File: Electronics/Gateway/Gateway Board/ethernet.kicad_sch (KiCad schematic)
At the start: 24 parts, among them IC6 LAN8742A-CZ-TR, J4 HR913129A, U1 USBLC6-4SC6-ES

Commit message: PCB Schematics finished
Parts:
- renumbered C18 to C401, C16 to C402, C17 to C403, C13 to C404, C19 to C405, C14 to C406, C15 to C407, FB1 to FB401, IC6 to IC401, J4 to J401, R22 to R401, R26 to R402, R27 to R403, R25 to R404, R32 to R405, R33 to R406, R21 to R407, R17 to R408, R18 to R409, R20 to R410, R19 to R411, R23 to R412, R24 to R413

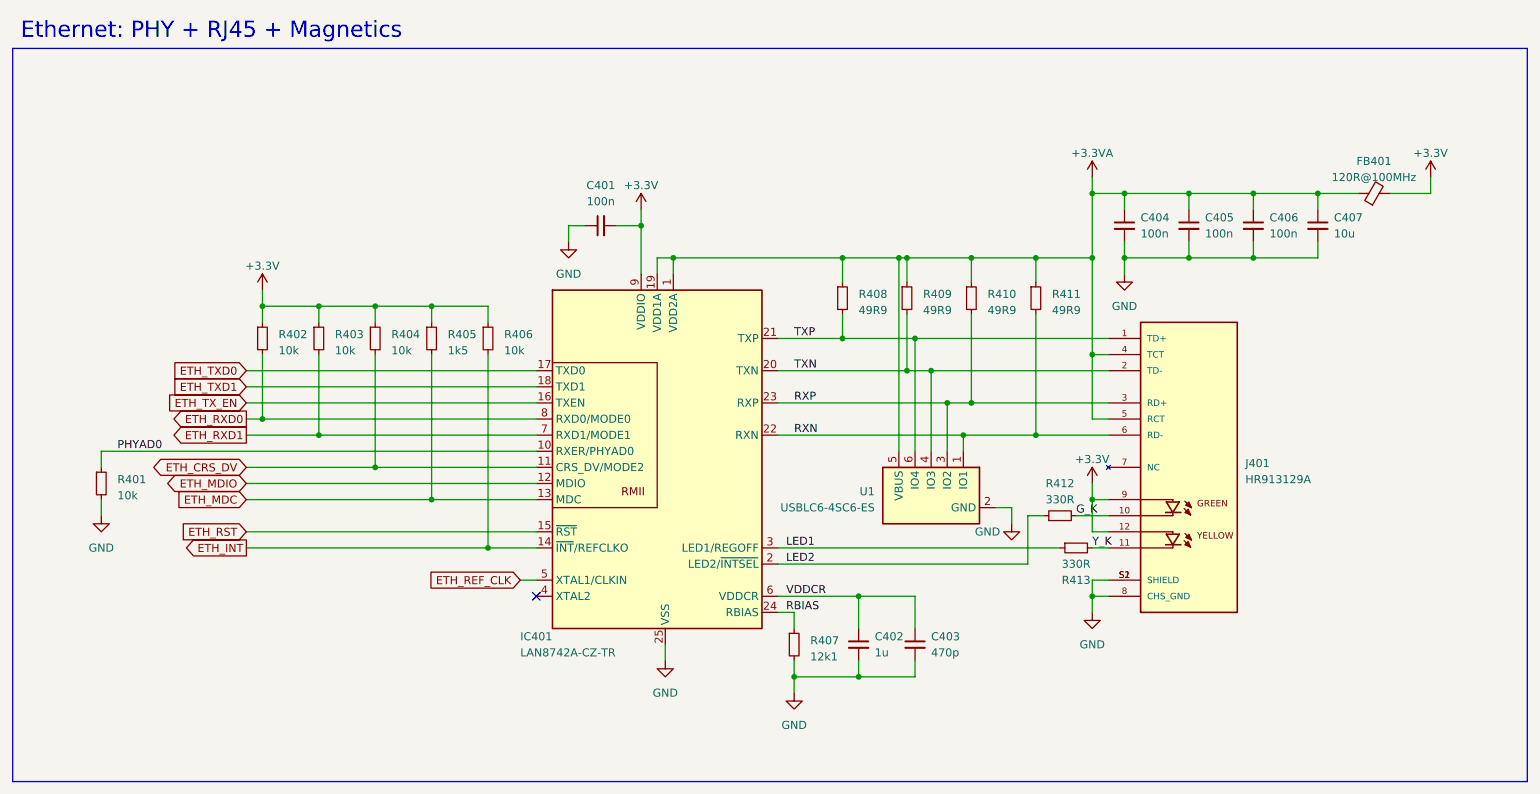
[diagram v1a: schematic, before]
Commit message: Gateway board layout complete and routing begun
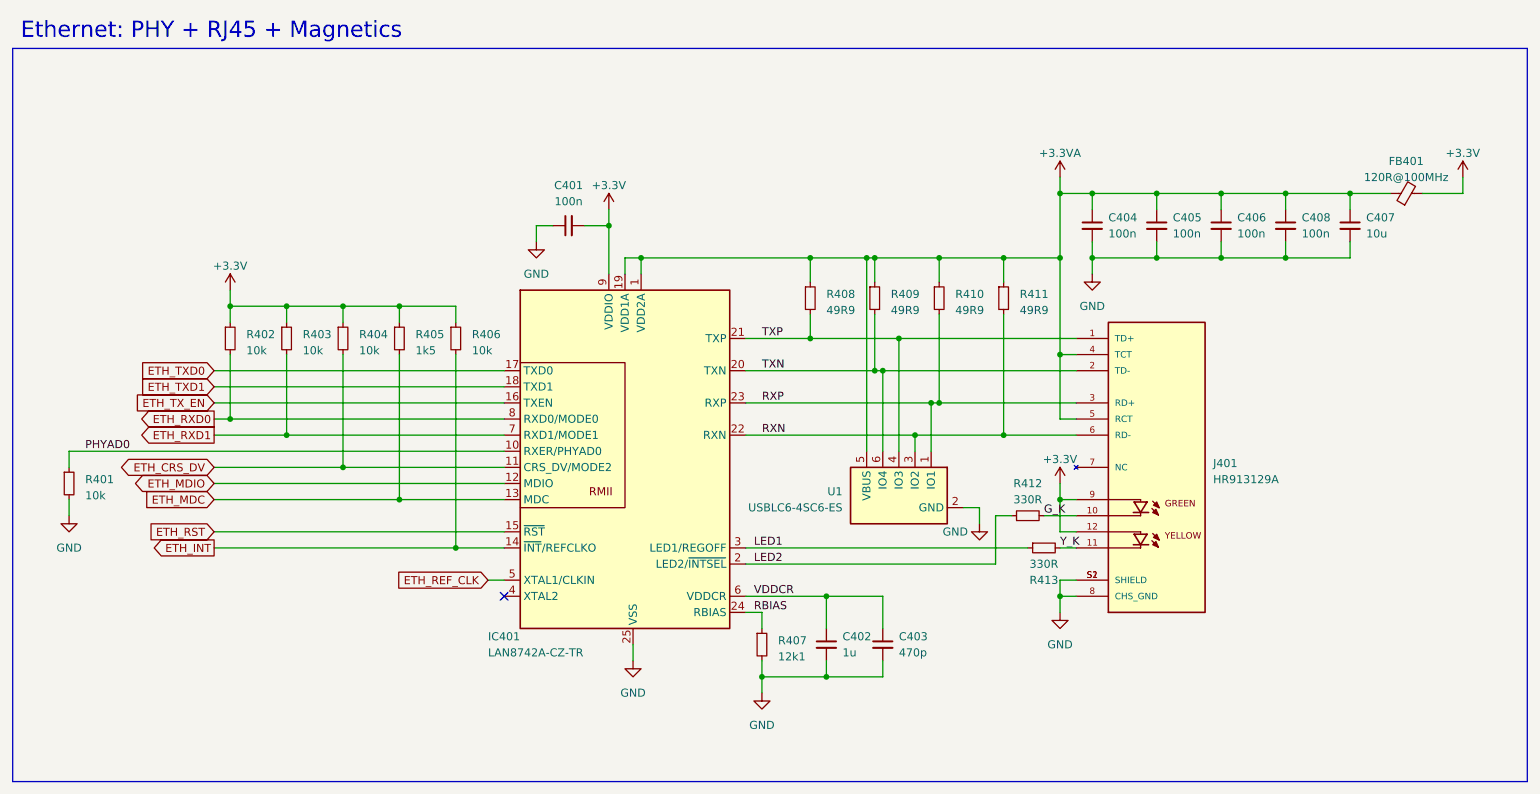
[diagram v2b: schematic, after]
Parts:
- added C408: 100n, Capacitor_SMD:C_0402_1005Metric, symbol Device:C_Small
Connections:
- net +3.3VA: now also C408.1
- net GND: now also C408.2
- net RXN: now also U1.3 (IO2); no longer U1.1 (IO1)
- net RXP: now also U1.1 (IO1); no longer U1.3 (IO2)
- net TXN: now also U1.6 (IO4); no longer U1.4 (IO3)
- net TXP: now also U1.4 (IO3); no longer U1.6 (IO4)
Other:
- moved on the sheet: C401, C402, C403, C404, C405, C406, C407, FB401, IC401, J401, R401, R402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

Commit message: Sensor hub board done
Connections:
- net ETH_MDC: no longer R405.2
- net ETH_MDIO: now also R405.2
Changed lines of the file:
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@@
   (junction (at 199.39 58.42) (diameter 0) (color 0 0 0 0)
   )
+  (junction (at 90.17 104.14) (diameter 0) (color 0 0 0 0)
+  )
   (junction (at 175.26 91.44) (diameter 0) (color 0 0 0 0)
-  )
-  (junction (at 90.17 106.68) (diameter 0) (color 0 0 0 0)
   )
   (junction (at 173.99 91.44) (diameter 0) (color 0 0 0 0)
@@
     (stroke (width 0) (type default))
   )
-  (wire (pts (xy 60.96 106.68) (xy 90.17 106.68))
-    (stroke (width 0) (type default))
-  )
   (wire (pts (xy 219.71 58.42) (xy 229.87 58.42))
     (stroke (width 0) (type default))
@@
     (stroke (width 0) (type default))
   )
+  (wire (pts (xy 90.17 83.82) (xy 90.17 104.14))
+    (stroke (width 0) (type default))
+  )
   (wire (pts (xy 166.37 134.62) (xy 157.48 134.62))
     (stroke (width 0) (type default))
@@
     (stroke (width 0) (type default))
   )
+  (wire (pts (xy 90.17 104.14) (xy 106.68 104.14))
+    (stroke (width 0) (type default))
+  )
   (wire (pts (xy 185.42 96.52) (xy 196.85 96.52))
     (stroke (width 0) (type default))
@@
     (stroke (width 0) (type default))
   )
-  (wire (pts (xy 60.96 104.14) (xy 106.68 104.14))
+  (wire (pts (xy 60.96 104.14) (xy 90.17 104.14))
     (stroke (width 0) (type default))
   )
@@
     (stroke (width 0) (type default))
   )
-  (wire (pts (xy 90.17 106.68) (xy 106.68 106.68))
+  (wire (pts (xy 60.96 106.68) (xy 106.68 106.68))
     (stroke (width 0) (type default))
   )
@@
     (stroke (width 0) (type default))
   )
-  (wire (pts (xy 90.17 83.82) (xy 90.17 106.68))
-    (stroke (width 0) (type default))
-  )
